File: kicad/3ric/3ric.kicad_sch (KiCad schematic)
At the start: 34 parts, among them SW1 SW_Push

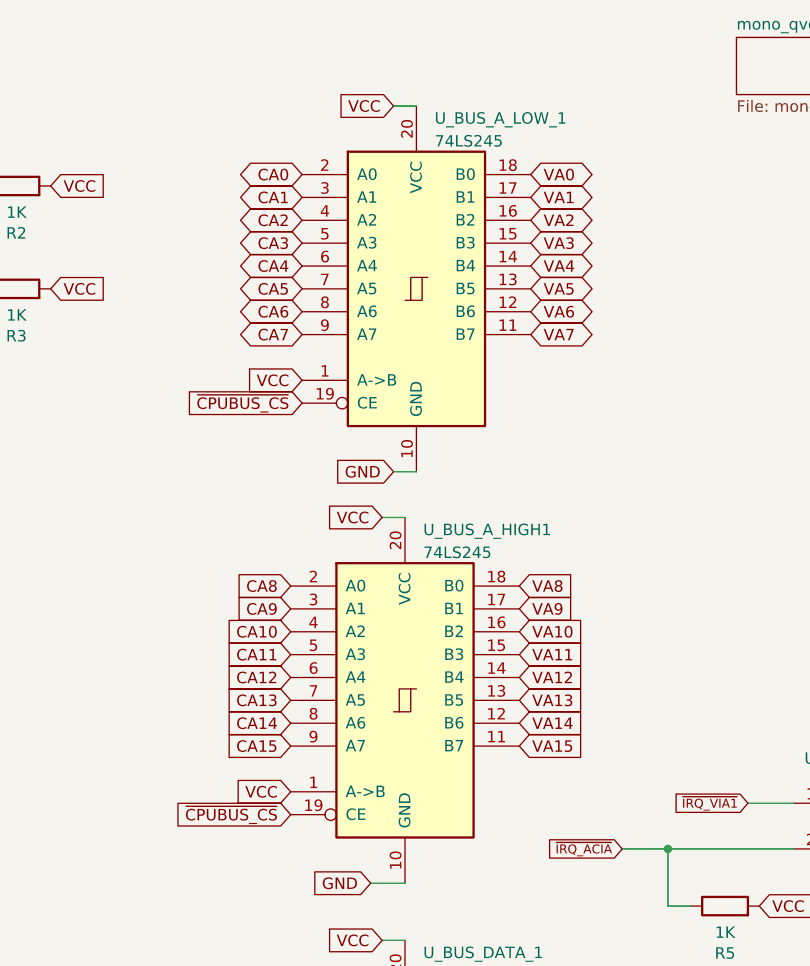
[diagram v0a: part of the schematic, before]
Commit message: adjustments to simplify breadboard bring up
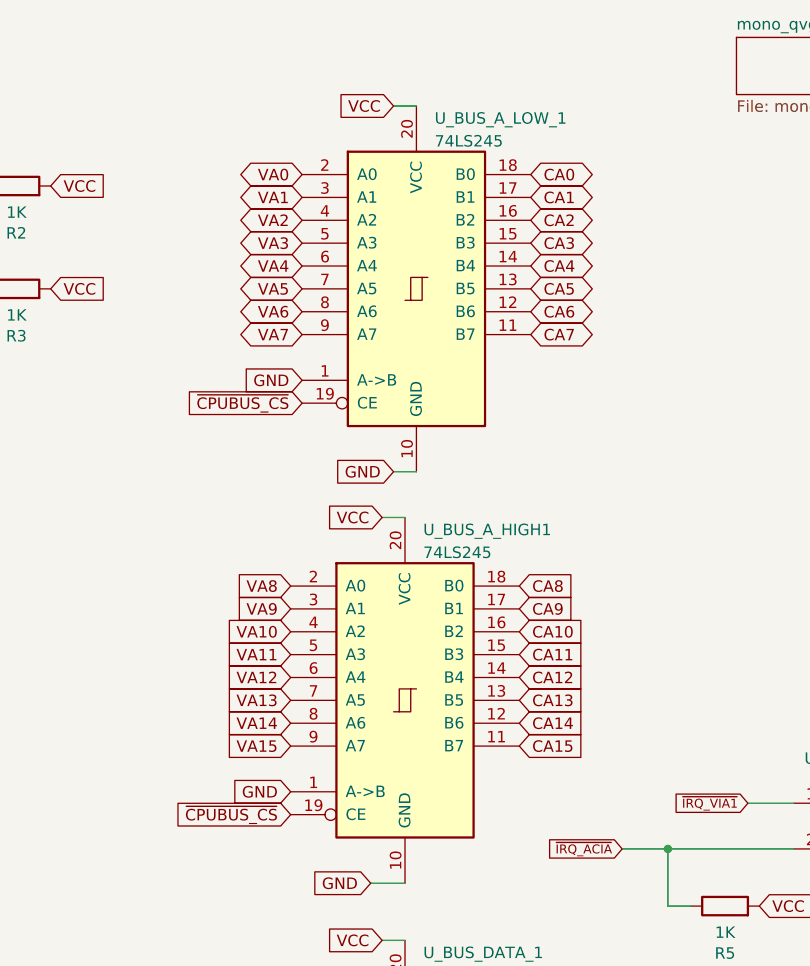
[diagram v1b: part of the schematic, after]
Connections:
- net CA0: now also U_BUS_A_LOW_1.18 (B0); no longer U_BUS_A_LOW_1.2 (A0)
- net CA1: now also U_BUS_A_LOW_1.17 (B1); no longer U_BUS_A_LOW_1.3 (A1)
- net CA10: now also U_BUS_A_HIGH1.16 (B2); no longer U_BUS_A_HIGH1.4 (A2)
- net CA11: now also U_BUS_A_HIGH1.15 (B3); no longer U_BUS_A_HIGH1.5 (A3)
- net CA12: now also U_BUS_A_HIGH1.14 (B4); no longer U_BUS_A_HIGH1.6 (A4)
- net CA13: now also U_BUS_A_HIGH1.13 (B5); no longer U_BUS_A_HIGH1.7 (A5)
- net CA14: now also U_BUS_A_HIGH1.12 (B6); no longer U_BUS_A_HIGH1.8 (A6)
- net CA15: now also U_BUS_A_HIGH1.11 (B7); no longer U_BUS_A_HIGH1.9 (A7)
- net CA2: now also U_BUS_A_LOW_1.16 (B2); no longer U_BUS_A_LOW_1.4 (A2)
- net CA3: now also U_BUS_A_LOW_1.15 (B3); no longer U_BUS_A_LOW_1.5 (A3)
- net CA4: now also U_BUS_A_LOW_1.14 (B4); no longer U_BUS_A_LOW_1.6 (A4)
- net CA5: now also U_BUS_A_LOW_1.13 (B5); no longer U_BUS_A_LOW_1.7 (A5)
- net CA6: now also U_BUS_A_LOW_1.12 (B6); no longer U_BUS_A_LOW_1.8 (A6)
- net CA7: now also U_BUS_A_LOW_1.11 (B7); no longer U_BUS_A_LOW_1.9 (A7)
- net CA8: now also U_BUS_A_HIGH1.18 (B0); no longer U_BUS_A_HIGH1.2 (A0)
- net CA9: now also U_BUS_A_HIGH1.17 (B1); no longer U_BUS_A_HIGH1.3 (A1)
- net GND: now also U_BUS_A_HIGH1.1 (A->B), U_BUS_A_LOW_1.1 (A->B)
- net VA0: now also U_BUS_A_LOW_1.2 (A0); no longer U_BUS_A_LOW_1.18 (B0)
- net VA1: now also U_BUS_A_LOW_1.3 (A1); no longer U_BUS_A_LOW_1.17 (B1)
- net VA10: now also U_BUS_A_HIGH1.4 (A2); no longer U_BUS_A_HIGH1.16 (B2)
- net VA11: now also U_BUS_A_HIGH1.5 (A3); no longer U_BUS_A_HIGH1.15 (B3)
- net VA12: now also U_BUS_A_HIGH1.6 (A4); no longer U_BUS_A_HIGH1.14 (B4)
- net VA13: now also U_BUS_A_HIGH1.7 (A5); no longer U_BUS_A_HIGH1.13 (B5)
- net VA14: now also U_BUS_A_HIGH1.8 (A6); no longer U_BUS_A_HIGH1.12 (B6)
- net VA15: now also U_BUS_A_HIGH1.9 (A7); no longer U_BUS_A_HIGH1.11 (B7)
- net VA2: now also U_BUS_A_LOW_1.4 (A2); no longer U_BUS_A_LOW_1.16 (B2)
- net VA3: now also U_BUS_A_LOW_1.5 (A3); no longer U_BUS_A_LOW_1.15 (B3)
- net VA4: now also U_BUS_A_LOW_1.6 (A4); no longer U_BUS_A_LOW_1.14 (B4)
- net VA5: now also U_BUS_A_LOW_1.7 (A5); no longer U_BUS_A_LOW_1.13 (B5)
- net VA6: now also U_BUS_A_LOW_1.8 (A6); no longer U_BUS_A_LOW_1.12 (B6)
- net VA7: now also U_BUS_A_LOW_1.9 (A7); no longer U_BUS_A_LOW_1.11 (B7)
- net VA8: now also U_BUS_A_HIGH1.2 (A0); no longer U_BUS_A_HIGH1.18 (B0)
- net VA9: now also U_BUS_A_HIGH1.3 (A1); no longer U_BUS_A_HIGH1.17 (B1)
- net VCC: no longer U_BUS_A_HIGH1.1 (A->B), U_BUS_A_LOW_1.1 (A->B)

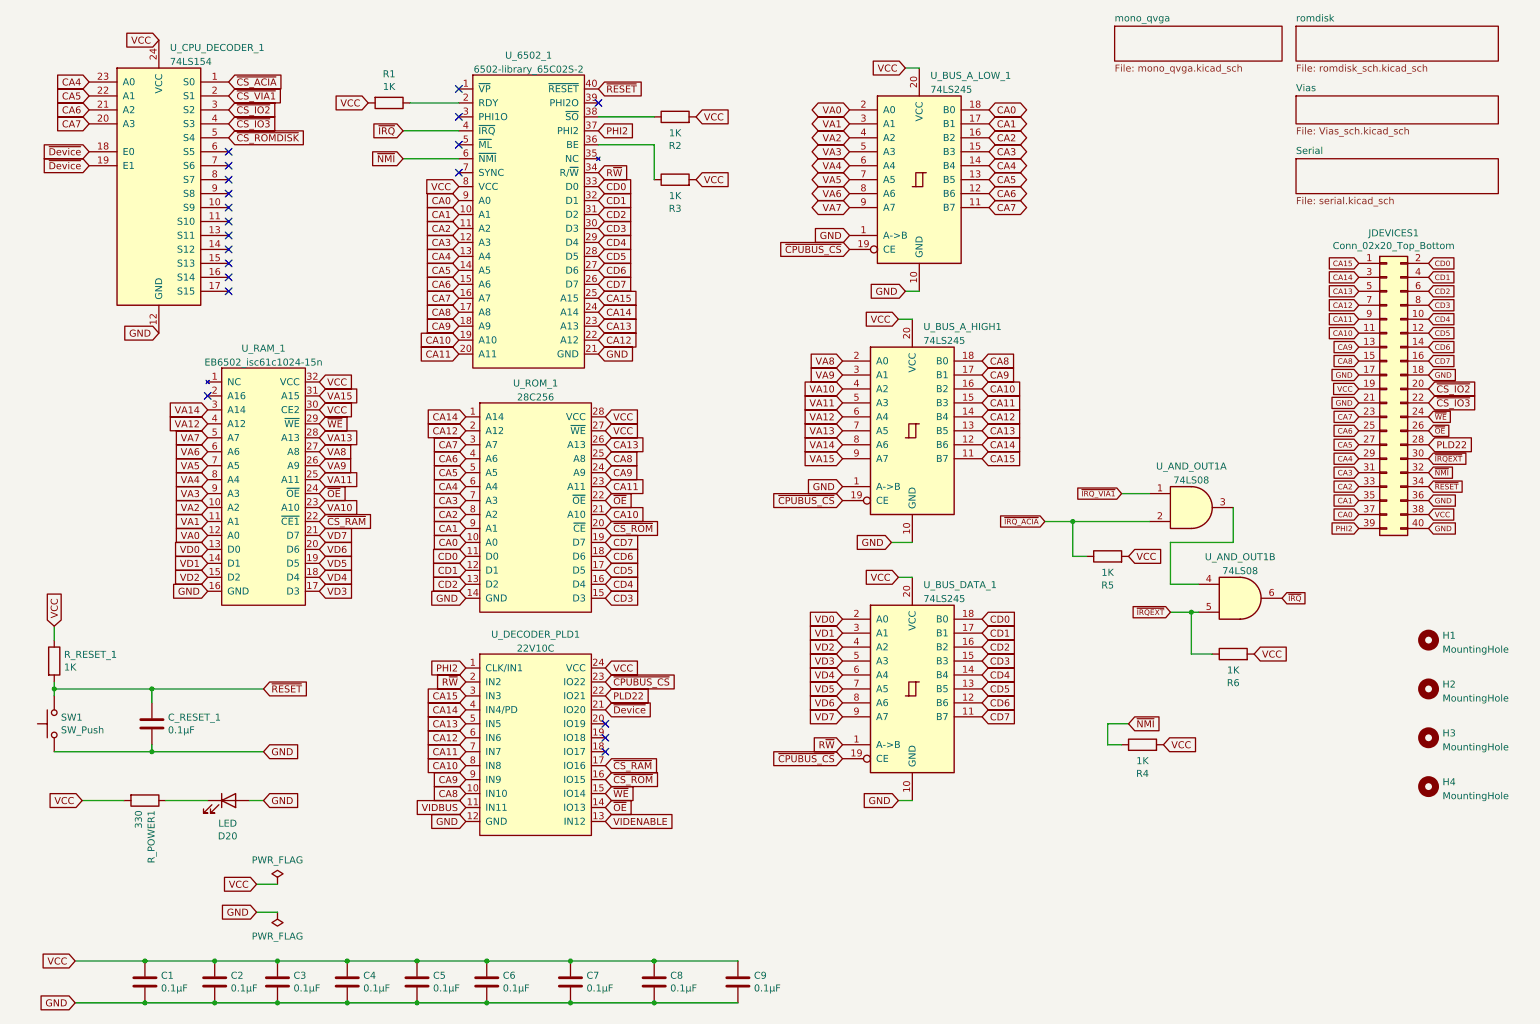
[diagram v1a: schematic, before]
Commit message: schematic updates - bring the schematics up to match breadboard changes current state has high res Apple II color emulation working
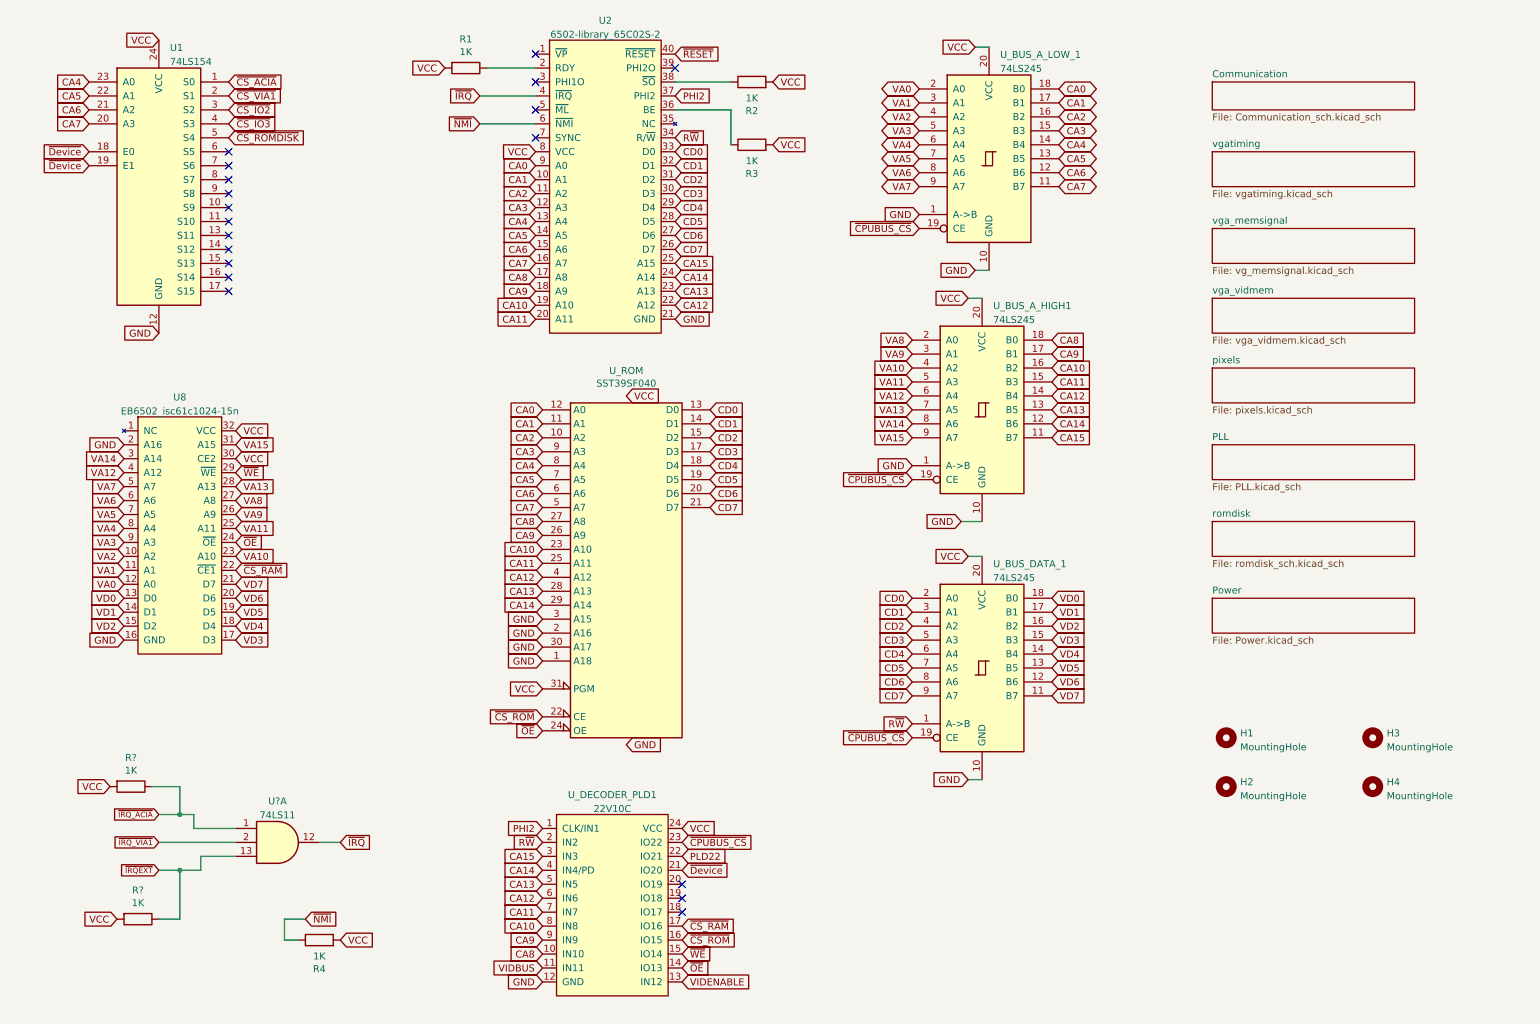
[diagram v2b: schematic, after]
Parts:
- removed C1, C2, C3, C4, C5, C6, C7, C8, C9, C_RESET_1: 0.1µF, Capacitor_THT:C_Axial_L3.8mm_D2.6mm_P7.50mm_Horizontal, symbol Device:C
- removed D20: LED, LED_THT:LED_D5.0mm, symbol Device:LED
- removed JDEVICES1: Conn_02x20_Top_Bottom, Connector_IDC:IDC-Header_2x20_P2.54mm_Vertical, symbol Connector_Generic:Conn_02x20_Odd_Even
- removed R5, R6, R_RESET_1: 1K, Resistor_THT:R_Axial_DIN0207_L6.3mm_D2.5mm_P7.62mm_Horizontal, symbol Device:R
- removed R_POWER1: 330, Resistor_THT:R_Axial_DIN0207_L6.3mm_D2.5mm_P7.62mm_Horizontal, symbol Device:R
- removed SW1: SW_Push, Button_Switch_THT:SW_PUSH_6mm, symbol Switch:SW_Push
- removed U_AND_OUT1: 74LS08, Package_DIP:DIP-14_W7.62mm_Socket, symbol 74xx:74LS08
- removed U_ROM_1: 28C256, Package_DIP:DIP-28_W15.24mm_Socket, symbol 6502:28C256
- added R? (x2): 1K, Resistor_THT:R_Axial_DIN0207_L6.3mm_D2.5mm_P7.62mm_Horizontal, symbol Device:R
- added U?: 74LS11, symbol 74xx:74LS11
- added U_ROM: SST39SF040, Package_DIP:DIP-32_W15.24mm_Socket, symbol Memory_Flash:SST39SF040
- renumbered U_CPU_DECODER_1 to U1, U_6502_1 to U2, U_RAM_1 to U8
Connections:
- net CA0: now also U_ROM.12 (A0)
- net CA1: now also U_ROM.11 (A1)
- net CA10: now also U_ROM.23 (A10)
- net CA11: now also U_ROM.25 (A11)
- net CA12: now also U_ROM.4 (A12)
- net CA13: now also U_ROM.28 (A13)
- net CA14: now also U_ROM.29 (A14)
- net CA2: now also U_ROM.10 (A2)
- net CA3: now also U_ROM.9 (A3)
- net CA4: now also U_ROM.8 (A4)
- net CA5: now also U_ROM.7 (A5)
- net CA6: now also U_ROM.6 (A6)
- net CA7: now also U_ROM.5 (A7)
- net CA8: now also U_ROM.27 (A8)
- net CA9: now also U_ROM.26 (A9)
- net CD0: now also U_BUS_DATA_1.2 (A0), U_ROM.13 (D0); no longer U_BUS_DATA_1.18 (B0)
- net CD1: now also U_BUS_DATA_1.3 (A1), U_ROM.14 (D1); no longer U_BUS_DATA_1.17 (B1)
- net CD2: now also U_BUS_DATA_1.4 (A2), U_ROM.15 (D2); no longer U_BUS_DATA_1.16 (B2)
- net CD3: now also U_BUS_DATA_1.5 (A3), U_ROM.17 (D3); no longer U_BUS_DATA_1.15 (B3)
- net CD4: now also U_BUS_DATA_1.6 (A4), U_ROM.18 (D4); no longer U_BUS_DATA_1.14 (B4)
- net CD5: now also U_BUS_DATA_1.7 (A5), U_ROM.19 (D5); no longer U_BUS_DATA_1.13 (B5)
- net CD6: now also U_BUS_DATA_1.8 (A6), U_ROM.20 (D6); no longer U_BUS_DATA_1.12 (B6)
- net CD7: now also U_BUS_DATA_1.9 (A7), U_ROM.21 (D7); no longer U_BUS_DATA_1.11 (B7)
- net GND: now also U8.2 (A16), U_ROM.1 (A18), U_ROM.16 (GND), U_ROM.2 (A16), U_ROM.3 (A15), U_ROM.30 (A17)
- net VCC: now also R?.2, R?.2, U_ROM.31 (PGM), U_ROM.32 (VCC)
- net VD0: now also U_BUS_DATA_1.18 (B0); no longer U_BUS_DATA_1.2 (A0)
- net VD1: now also U_BUS_DATA_1.17 (B1); no longer U_BUS_DATA_1.3 (A1)
- net VD2: now also U_BUS_DATA_1.16 (B2); no longer U_BUS_DATA_1.4 (A2)
- net VD3: now also U_BUS_DATA_1.15 (B3); no longer U_BUS_DATA_1.5 (A3)
- net VD4: now also U_BUS_DATA_1.14 (B4); no longer U_BUS_DATA_1.6 (A4)
- net VD5: now also U_BUS_DATA_1.13 (B5); no longer U_BUS_DATA_1.7 (A5)
- net VD6: now also U_BUS_DATA_1.12 (B6); no longer U_BUS_DATA_1.8 (A6)
- net VD7: now also U_BUS_DATA_1.11 (B7); no longer U_BUS_DATA_1.9 (A7)
- net ~{CS_ROM}: now also U_ROM.22 (CE)
- net ~{IRQEXT}: now also R?.1, U?.13
- net ~{IRQ_ACIA}: now also R?.1, U?.1
- net ~{IRQ_VIA1}: now also U?.2
- net ~{IRQ}: now also U?.12
- net ~{OE}: now also U_ROM.24 (OE)
- no-connect marks 20 -> 19
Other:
- sheet Vias renamed Communication
- removed sheet Serial
- removed sheet mono_qvga
- added sheet PLL (PLL.kicad_sch)
- added sheet Power (Power.kicad_sch)
- added sheet pixels (pixels.kicad_sch)
- added sheet vga_memsignal (vg_memsignal.kicad_sch)
- added sheet vga_vidmem (vga_vidmem.kicad_sch)
- added sheet vgatiming (vgatiming.kicad_sch)
- sheet Communication: file Vias_sch.kicad_sch -> Communication_sch.kicad_sch
- moved on the sheet: H1, H2, H3, H4, R1, R2, R3, R4, U2, U8, U_BUS_A_HIGH1, U_BUS_A_LOW_1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

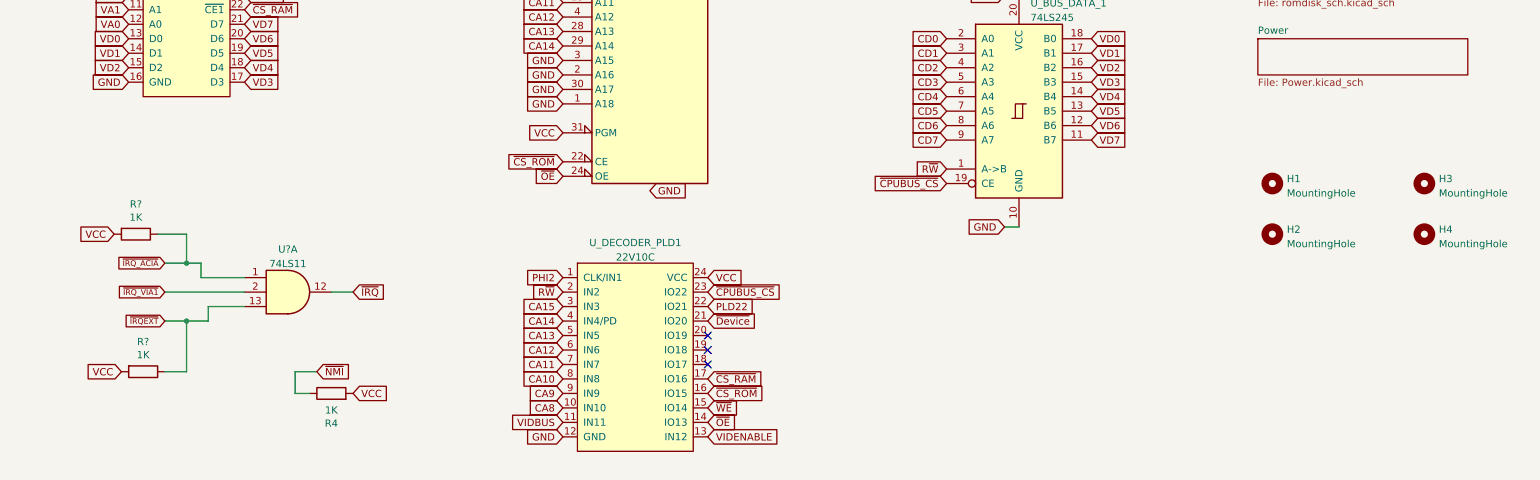
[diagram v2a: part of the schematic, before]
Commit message: stash latest simulation and schematic changes - adding untested soft switches and RAM banking
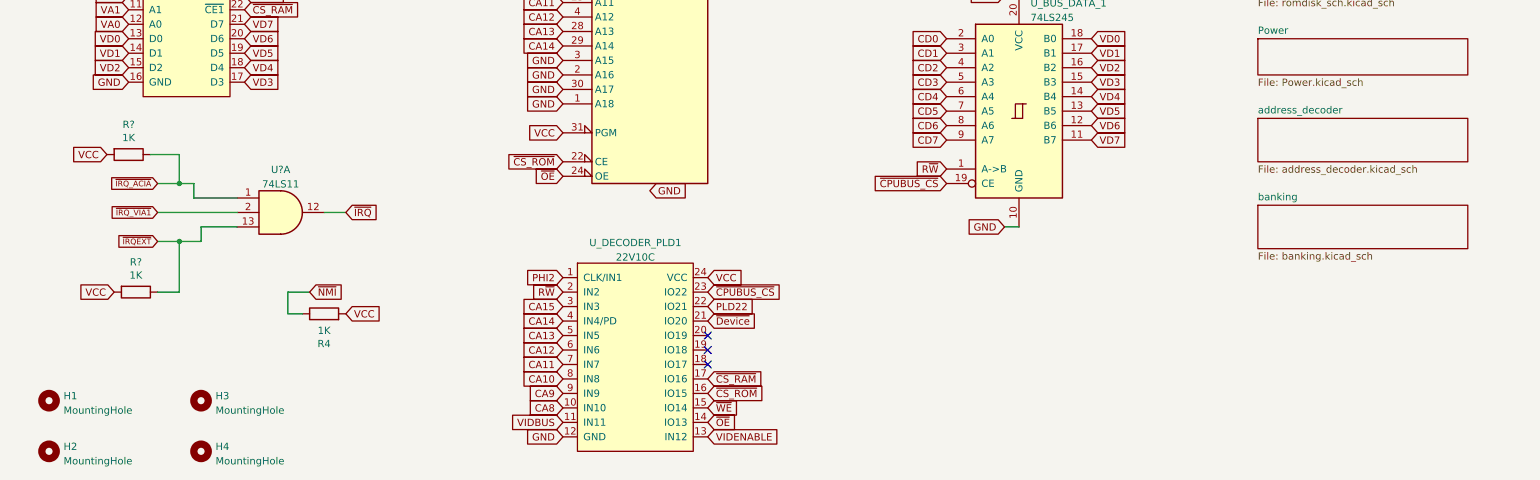
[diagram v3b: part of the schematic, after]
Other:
- added sheet address_decoder (address_decoder.kicad_sch)
- added sheet banking (banking.kicad_sch)
- moved on the sheet: H1, H2, H3, H4, R4, R?, U?A

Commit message: updates to logisim project and schematics
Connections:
- net CA10: no longer U_DECODER_PLD1.8 (IN8)
- net CA15: now also U_ROM.3 (A15)
- net CA8: no longer U_DECODER_PLD1.10 (IN10)
- net CA9: no longer U_DECODER_PLD1.9 (IN9)
- net GND: no longer U8.2 (A16), U_ROM.3 (A15)
- net ~{CPUBUS_CS}: now also U_DECODER_PLD1.20 (IO19); no longer U_DECODER_PLD1.23 (IO22)
- net ~{CS_ACIA}: now also U1.2 (S1); no longer U1.1 (S0)
- net ~{CS_IO2}: now also U1.4 (S3); no longer U1.3 (S2)
- net ~{CS_IO3}: now also U1.5 (S4); no longer U1.4 (S3)
- net ~{CS_ROMDISK}: now also U1.6 (S5); no longer U1.5 (S4)
- net ~{CS_VIA1}: now also U1.3 (S2); no longer U1.2 (S1)
- net A16: now reaches U_DECODER_PLD1.19 (IO18)
- net A16: now also U8.2 (A16)
- net PLD22 renamed RAMREAD
- new net B2: U_DECODER_PLD1.9 (IN9)
- new net BB: U_DECODER_PLD1.8 (IN8)
- new net RAMWRITE: U_DECODER_PLD1.10 (IN10)
- no-connect marks 19 -> 18
